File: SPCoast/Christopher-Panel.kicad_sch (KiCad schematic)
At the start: 23 parts, among them U10028 0x27, U10029 0x28, U10030 0x29

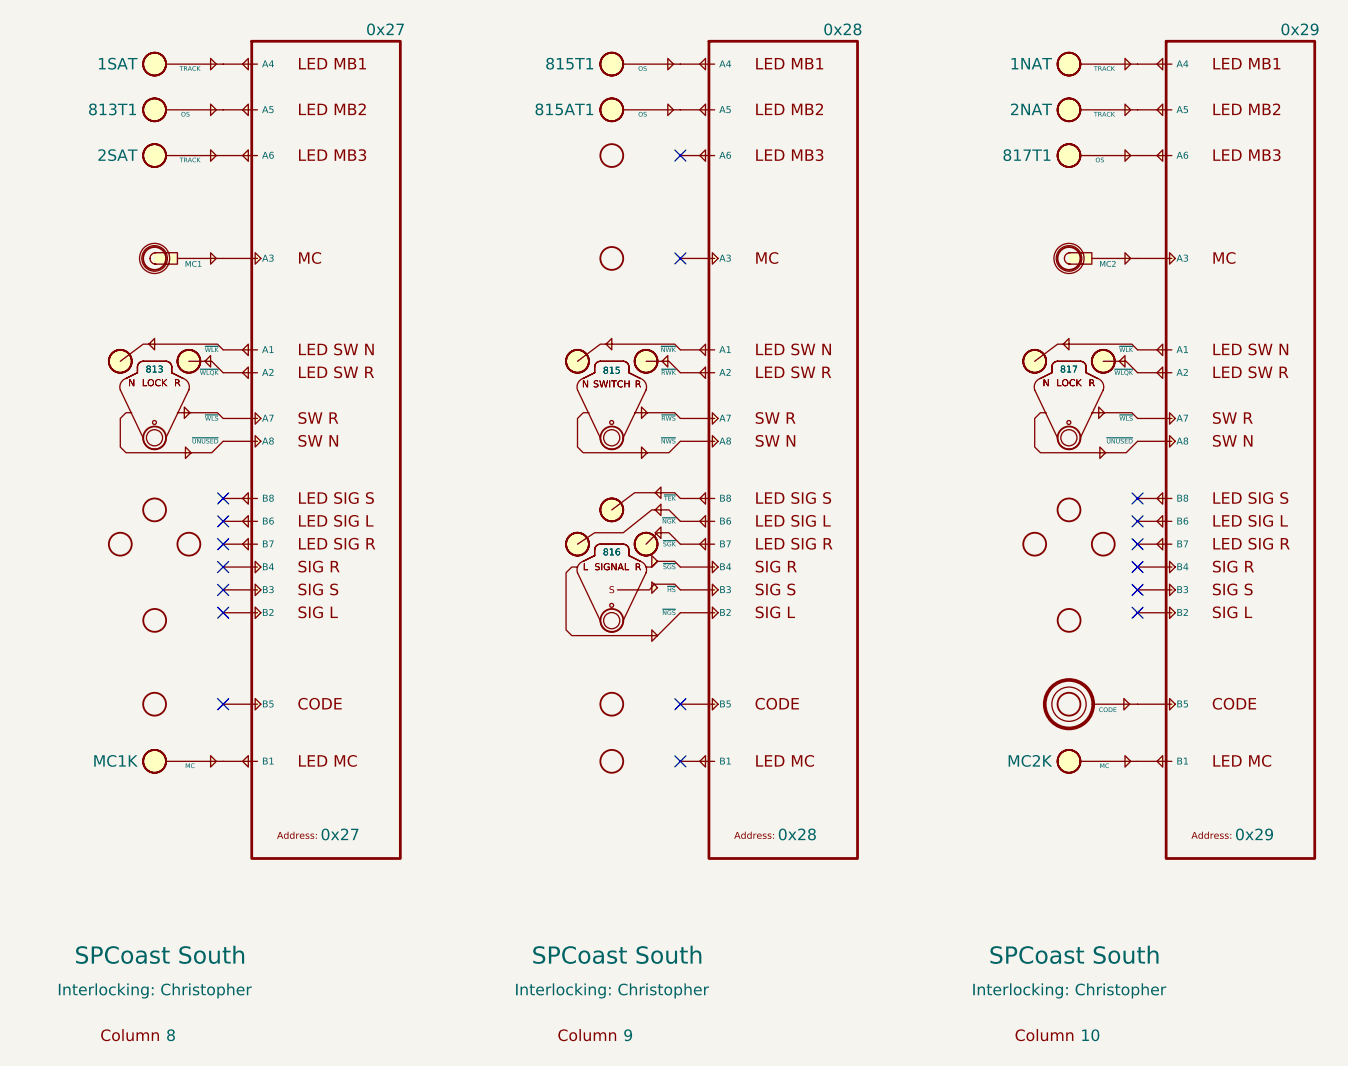
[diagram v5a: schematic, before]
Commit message: chore(kicad): owner edits: GPIO drivers carry Address, Sargent I2C addresses, CMRI body text from fields
Baseline of the owner's saved work before the ADR 0005 scripts:
- Driver-GPIO-Digital and Driver-GPIO-Pixel gain an Address field (the
  board pin); Value renders ${Address}; body text and arrow adjusted.
- Driver-CMRI-IB/OB body text renders UA${Address}.IN/OUT.${Bit} from
  the fields instead of ${VALUE}.
- Sargent, Gilroy Interchange and Luchessa GPIO instances carry Address;
  Sargent Exp2 back at 0x26, Exp3 0x27.
- All sheets resaved by KiCad 10 (reordering), project file
  used_designators cleared by KiCad.

Verified: no lock files; committed as saved, unverified by netlist (the
baseline netlist is exported in the next step).

Co-Authored-By: Claude Fable 5.1 <noreply@anthropic.com>
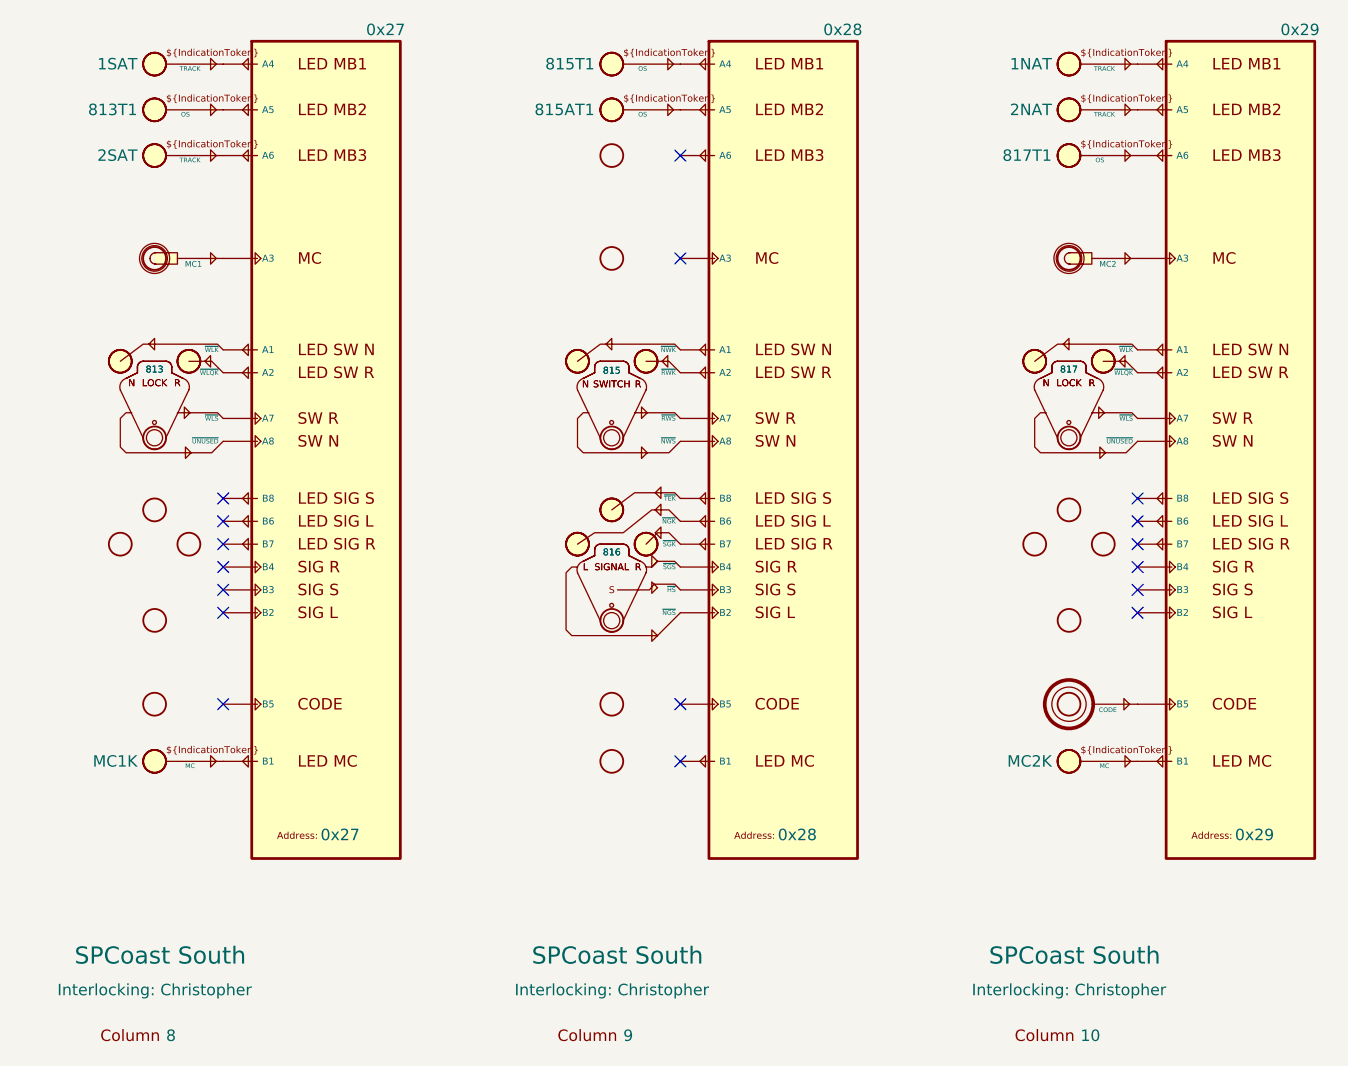
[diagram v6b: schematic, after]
